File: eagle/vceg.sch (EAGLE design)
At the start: 58 parts, among them IC1 4052N, IC2 4001N, IC3 TL074P, IC4 CA3080E, Q1 2N3906INLINE, Q2 2N3906INLINE, U1 POWER

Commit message: starting on a board
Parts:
- renumbered R1 to REL_POT, R10 to ATT_POT, R13 to SUS_POT, R4 to RATE_POT, R7 to DEC_POT
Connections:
- new net N$40: IC3D.-IN, IC3D.OUT
- net GND: now also IC3D.+IN
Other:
- moved on the sheet: IC3D
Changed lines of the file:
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@@
 <part name="P-1" library="supply1" deviceset="-12V" device=""/>
 <part name="GND1" library="supply1" deviceset="GND" device=""/>
-<part name="R4" library="pot" deviceset="3RP/1610N" device="" value="50k"/>
+<part name="RATE_POT" library="pot" deviceset="3RP/1610N" device="" value="50k"/>
 <part name="RATE" library="solpad" deviceset="LSP10" device=""/>
 <part name="R5" library="SparkFun-Resistors" deviceset="RESISTOR" device="PTH-1/4W" value="120k"/>
@@
 <part name="GND3" library="supply1" deviceset="GND" device=""/>
 <part name="P+3" library="supply1" deviceset="+12V" device=""/>
-<part name="R1" library="pot" deviceset="3RP/1610N" device="" value="50k"/>
+<part name="REL_POT" library="pot" deviceset="3RP/1610N" device="" value="50k"/>
 <part name="RELEASE" library="solpad" deviceset="LSP10" device=""/>
 <part name="R2" library="SparkFun-Resistors" deviceset="RESISTOR" device="PTH-1/4W" value="120k"/>
@@
 <part name="GND2" library="supply1" deviceset="GND" device=""/>
 <part name="P+2" library="supply1" deviceset="+12V" device=""/>
-<part name="R7" library="pot" deviceset="3RP/1610N" device="" value="50k"/>
+<part name="DEC_POT" library="pot" deviceset="3RP/1610N" device="" value="50k"/>
 <part name="DECAY" library="solpad" deviceset="LSP10" device=""/>
 <part name="R8" library="SparkFun-Resistors" deviceset="RESISTOR" device="PTH-1/4W" value="120k"/>
@@
 <part name="GND4" library="supply1" deviceset="GND" device=""/>
 <part name="P+4" library="supply1" deviceset="+12V" device=""/>
-<part name="R10" library="pot" deviceset="3RP/1610N" device="" value="50k"/>
+<part name="ATT_POT" library="pot" deviceset="3RP/1610N" device="" value="50k"/>
 <part name="ATTACK" library="solpad" deviceset="LSP10" device=""/>
 <part name="R11" library="SparkFun-Resistors" deviceset="RESISTOR" device="PTH-1/4W" value="150k"/>
@@
 <part name="GND5" library="supply1" deviceset="GND" device=""/>
 <part name="P+5" library="supply1" deviceset="+12V" device=""/>
-<part name="R13" library="pot" deviceset="3RP/1610N" device="" value="50k"/>
+<part name="SUS_POT" library="pot" deviceset="3RP/1610N" device="" value="50k"/>
 <part name="SUSTAIN" library="solpad" deviceset="LSP10" device=""/>
 <part name="R14" library="SparkFun-Resistors" deviceset="RESISTOR" device="PTH-1/4W" value="220k"/>
@@
 <part name="TG_SWA_1" library="solpad" deviceset="LSP10" device=""/>
 <part name="GATE_NORMAL" library="solpad" deviceset="LSP10" device=""/>
+<part name="GND20" library="supply1" deviceset="GND" device=""/>
 </parts>
 <sheets>
@@
 <instance part="IC3" gate="B" x="135.636" y="17.78" rot="R180"/>
 <instance part="IC3" gate="C" x="135.636" y="-10.922" rot="R180"/>
-<instance part="IC3" gate="D" x="152.146" y="81.026" rot="MR180"/>
+<instance part="IC3" gate="D" x="153.416" y="90.424" rot="MR180"/>
 <instance part="U1" gate="G$1" x="42.926" y="93.98"/>
 <instance part="P+1" gate="1" x="66.04" y="106.68"/>
 <instance part="P-1" gate="1" x="66.04" y="91.44"/>
 <instance part="GND1" gate="1" x="76.2" y="93.98"/>
-<instance part="R4" gate="G$1" x="-12.7" y="86.36"/>
+<instance part="RATE_POT" gate="G$1" x="-12.7" y="86.36"/>
 <instance part="RATE" gate="1" x="-15.24" y="99.06" rot="R90"/>
 <instance part="R5" gate="G$1" x="-7.62" y="99.06"/>
@@
 <instance part="GND3" gate="1" x="-12.7" y="78.74"/>
 <instance part="P+3" gate="1" x="-12.7" y="93.98"/>
-<instance part="R1" gate="G$1" x="-12.7" y="55.88"/>
+<instance part="REL_POT" gate="G$1" x="-12.7" y="55.88"/>
 <instance part="RELEASE" gate="1" x="-15.24" y="68.58" rot="R90"/>
 <instance part="R2" gate="G$1" x="-7.62" y="68.58"/>
@@
 <instance part="GND2" gate="1" x="-12.7" y="48.26"/>
 <instance part="P+2" gate="1" x="-12.7" y="63.5"/>
-<instance part="R7" gate="G$1" x="-12.7" y="25.4"/>
+<instance part="DEC_POT" gate="G$1" x="-12.7" y="25.4"/>
 <instance part="DECAY" gate="1" x="-15.24" y="38.1" rot="R90"/>
 <instance part="R8" gate="G$1" x="-7.62" y="38.1"/>
@@
 <instance part="GND4" gate="1" x="-12.7" y="17.78"/>
 <instance part="P+4" gate="1" x="-12.7" y="33.02"/>
-<instance part="R10" gate="G$1" x="-12.7" y="-5.08"/>
+<instance part="ATT_POT" gate="G$1" x="-12.7" y="-5.08"/>
 <instance part="ATTACK" gate="1" x="-15.24" y="7.62" rot="R90"/>
 <instance part="R11" gate="G$1" x="-7.62" y="7.62"/>
@@
 <instance part="GND5" gate="1" x="-12.7" y="-12.7"/>
 <instance part="P+5" gate="1" x="-12.7" y="2.54"/>
-<instance part="R13" gate="G$1" x="-12.7" y="-35.56"/>
+<instance part="SUS_POT" gate="G$1" x="-12.7" y="-35.56"/>
 <instance part="SUSTAIN" gate="1" x="-15.24" y="-22.86" rot="R90"/>
 <instance part="R14" gate="G$1" x="-7.62" y="-22.86"/>
@@
 <instance part="TG_SWA_1" gate="1" x="29.21" y="12.7" rot="R90"/>
 <instance part="GATE_NORMAL" gate="1" x="59.944" y="83.82" rot="R270"/>
+<instance part="GND20" gate="1" x="145.796" y="82.55"/>
 </instances>
 <busses>
@@
 </segment>
 <segment>
-<pinref part="R4" gate="G$1" pin="A"/>
+<pinref part="RATE_POT" gate="G$1" pin="A"/>
 <pinref part="GND3" gate="1" pin="GND"/>
 </segment>
 <segment>
-<pinref part="R1" gate="G$1" pin="A"/>
+<pinref part="REL_POT" gate="G$1" pin="A"/>
 <pinref part="GND2" gate="1" pin="GND"/>
 </segment>
 <segment>
-<pinref part="R7" gate="G$1" pin="A"/>
+<pinref part="DEC_POT" gate="G$1" pin="A"/>
 <pinref part="GND4" gate="1" pin="GND"/>
 </segment>
 <segment>
-<pinref part="R10" gate="G$1" pin="A"/>
+<pinref part="ATT_POT" gate="G$1" pin="A"/>
 <pinref part="GND5" gate="1" pin="GND"/>
 </segment>
 <segment>
-<pinref part="R13" gate="G$1" pin="A"/>
+<pinref part="SUS_POT" gate="G$1" pin="A"/>
 <pinref part="GND6" gate="1" pin="GND"/>
 </segment>
@@
 <wire x1="12.7" y1="-41.402" x2="12.7" y2="-39.37" width="0.1524" layer="91"/>
 </segment>
+<segment>
+<pinref part="IC3" gate="D" pin="+IN"/>
+<pinref part="GND20" gate="1" pin="GND"/>
+<wire x1="145.796" y1="85.09" x2="145.796" y2="87.884" width="0.1524" layer="91"/>
+</segment>
 </net>
 <net name="+12V" class="0">
 <segment>
-<pinref part="R4" gate="G$1" pin="E"/>
+<pinref part="RATE_POT" gate="G$1" pin="E"/>
 <pinref part="P+3" gate="1" pin="+12V"/>
 </segment>
 <segment>
-<pinref part="R1" gate="G$1" pin="E"/>
+<pinref part="REL_POT" gate="G$1" pin="E"/>
 <pinref part="P+2" gate="1" pin="+12V"/>
 </segment>
 <segment>
-<pinref part="R7" gate="G$1" pin="E"/>
+<pinref part="DEC_POT" gate="G$1" pin="E"/>
 <pinref part="P+4" gate="1" pin="+12V"/>
 </segment>
 <segment>
-<pinref part="R10" gate="G$1" pin="E"/>
+<pinref part="ATT_POT" gate="G$1" pin="E"/>
 <pinref part="P+5" gate="1" pin="+12V"/>
 </segment>
 <segment>
-<pinref part="R13" gate="G$1" pin="E"/>
+<pinref part="SUS_POT" gate="G$1" pin="E"/>
 <pinref part="P+6" gate="1" pin="+12V"/>
 </segment>
@@
 <net name="N$6" class="0">
 <segment>
-<pinref part="R4" gate="G$1" pin="S"/>
+<pinref part="RATE_POT" gate="G$1" pin="S"/>
 <pinref part="R6" gate="G$1" pin="1"/>
 <wire x1="-7.62" y1="86.36" x2="-2.54" y2="86.36" width="0.1524" layer="91"/>
@@
 <net name="N$3" class="0">
 <segment>
-<pinref part="R1" gate="G$1" pin="S"/>
+<pinref part="REL_POT" gate="G$1" pin="S"/>
 <pinref part="R3" gate="G$1" pin="1"/>
 <wire x1="-7.62" y1="55.88" x2="-2.54" y2="55.88" width="0.1524" layer="91"/>
@@
 <net name="N$9" class="0">
 <segment>
-<pinref part="R7" gate="G$1" pin="S"/>
+<pinref part="DEC_POT" gate="G$1" pin="S"/>
 <pinref part="R9" gate="G$1" pin="1"/>
 <wire x1="-7.62" y1="25.4" x2="-2.54" y2="25.4" width="0.1524" layer="91"/>
@@
 <net name="N$12" class="0">
 <segment>
-<pinref part="R10" gate="G$1" pin="S"/>
+<pinref part="ATT_POT" gate="G$1" pin="S"/>
 <pinref part="R12" gate="G$1" pin="1"/>
 <wire x1="-7.62" y1="-5.08" x2="-2.54" y2="-5.08" width="0.1524" layer="91"/>
@@
 <net name="N$15" class="0">
 <segment>
-<pinref part="R13" gate="G$1" pin="S"/>
+<pinref part="SUS_POT" gate="G$1" pin="S"/>
 <pinref part="R15" gate="G$1" pin="1"/>
 <wire x1="-7.62" y1="-35.56" x2="-2.54" y2="-35.56" width="0.1524" layer="91"/>
@@
 </segment>
 </net>
+<net name="N$40" class="0">
+<segment>
+<pinref part="IC3" gate="D" pin="OUT"/>
+<wire x1="161.036" y1="90.424" x2="164.084" y2="90.424" width="0.1524" layer="91"/>
+<wire x1="164.084" y1="90.424" x2="164.084" y2="100.838" width="0.1524" layer="91"/>
+<wire x1="164.084" y1="100.838" x2="142.24" y2="100.838" width="0.1524" layer="91"/>
+<pinref part="IC3" gate="D" pin="-IN"/>
+<wire x1="142.24" y1="100.838" x2="142.24" y2="96.52" width="0.1524" layer="91"/>
+<wire x1="142.24" y1="96.52" x2="145.796" y2="92.964" width="0.1524" layer="91"/>
+</segment>
+</net>

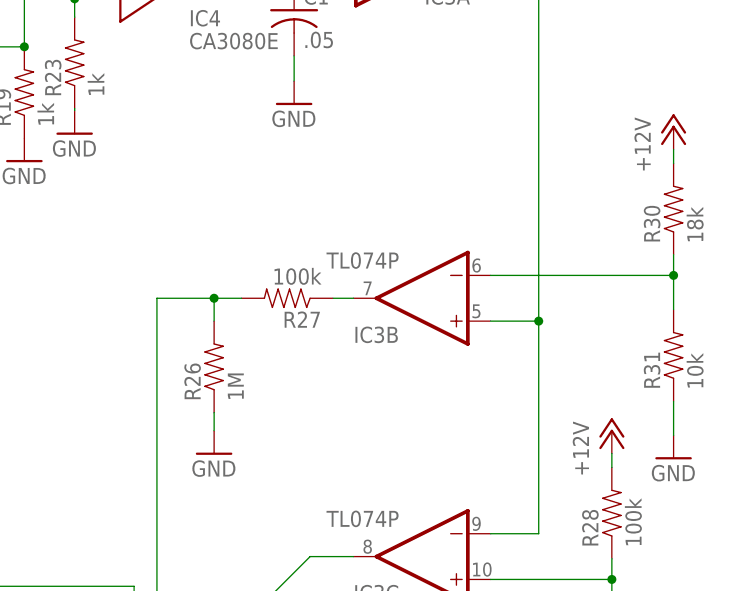
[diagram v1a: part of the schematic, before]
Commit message: remembered to power tl074
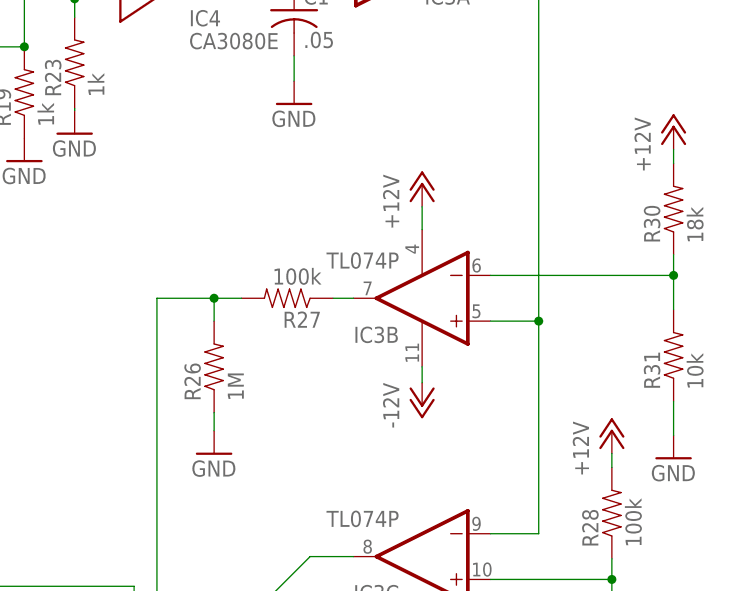
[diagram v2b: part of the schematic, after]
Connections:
- net +12V: now also IC3P.V+
- net -12V: now also IC3P.V-
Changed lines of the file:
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@@
 <part name="GATE_NORMAL" library="solpad" deviceset="LSP10" device=""/>
 <part name="GND20" library="supply1" deviceset="GND" device=""/>
+<part name="P+12" library="supply1" deviceset="+12V" device=""/>
+<part name="P-2" library="supply1" deviceset="-12V" device=""/>
 </parts>
 <sheets>
@@
 <instance part="GATE_NORMAL" gate="1" x="59.944" y="83.82" rot="R270"/>
 <instance part="GND20" gate="1" x="145.796" y="82.55"/>
+<instance part="IC3" gate="P" x="135.636" y="17.78"/>
+<instance part="P+12" gate="1" x="135.636" y="30.48"/>
+<instance part="P-2" gate="1" x="135.636" y="5.842"/>
 </instances>
 <busses>
@@
 <wire x1="25.4" y1="19.812" x2="25.4" y2="27.432" width="0.1524" layer="91"/>
 </segment>
+<segment>
+<pinref part="IC3" gate="P" pin="V+"/>
+<pinref part="P+12" gate="1" pin="+12V"/>
+<wire x1="135.636" y1="27.94" x2="135.636" y2="25.4" width="0.1524" layer="91"/>
+</segment>
 </net>
 <net name="-12V" class="0">
@@
 <wire x1="66.04" y1="93.98" x2="53.086" y2="93.98" width="0.1524" layer="91"/>
 </segment>
+<segment>
+<pinref part="IC3" gate="P" pin="V-"/>
+<pinref part="P-2" gate="1" pin="-12V"/>
+<wire x1="135.636" y1="8.382" x2="135.636" y2="10.16" width="0.1524" layer="91"/>
+</segment>
 </net>
